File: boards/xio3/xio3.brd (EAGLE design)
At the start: 170 x 100 mm, 352 parts, among them J1 12401598E4#2A, Q1 BSS138, Q2 BSS138, Q3 BC817-16LT3G, Q4 BC817-16LT3G, Y2 FA-238 25.0000MB-K3

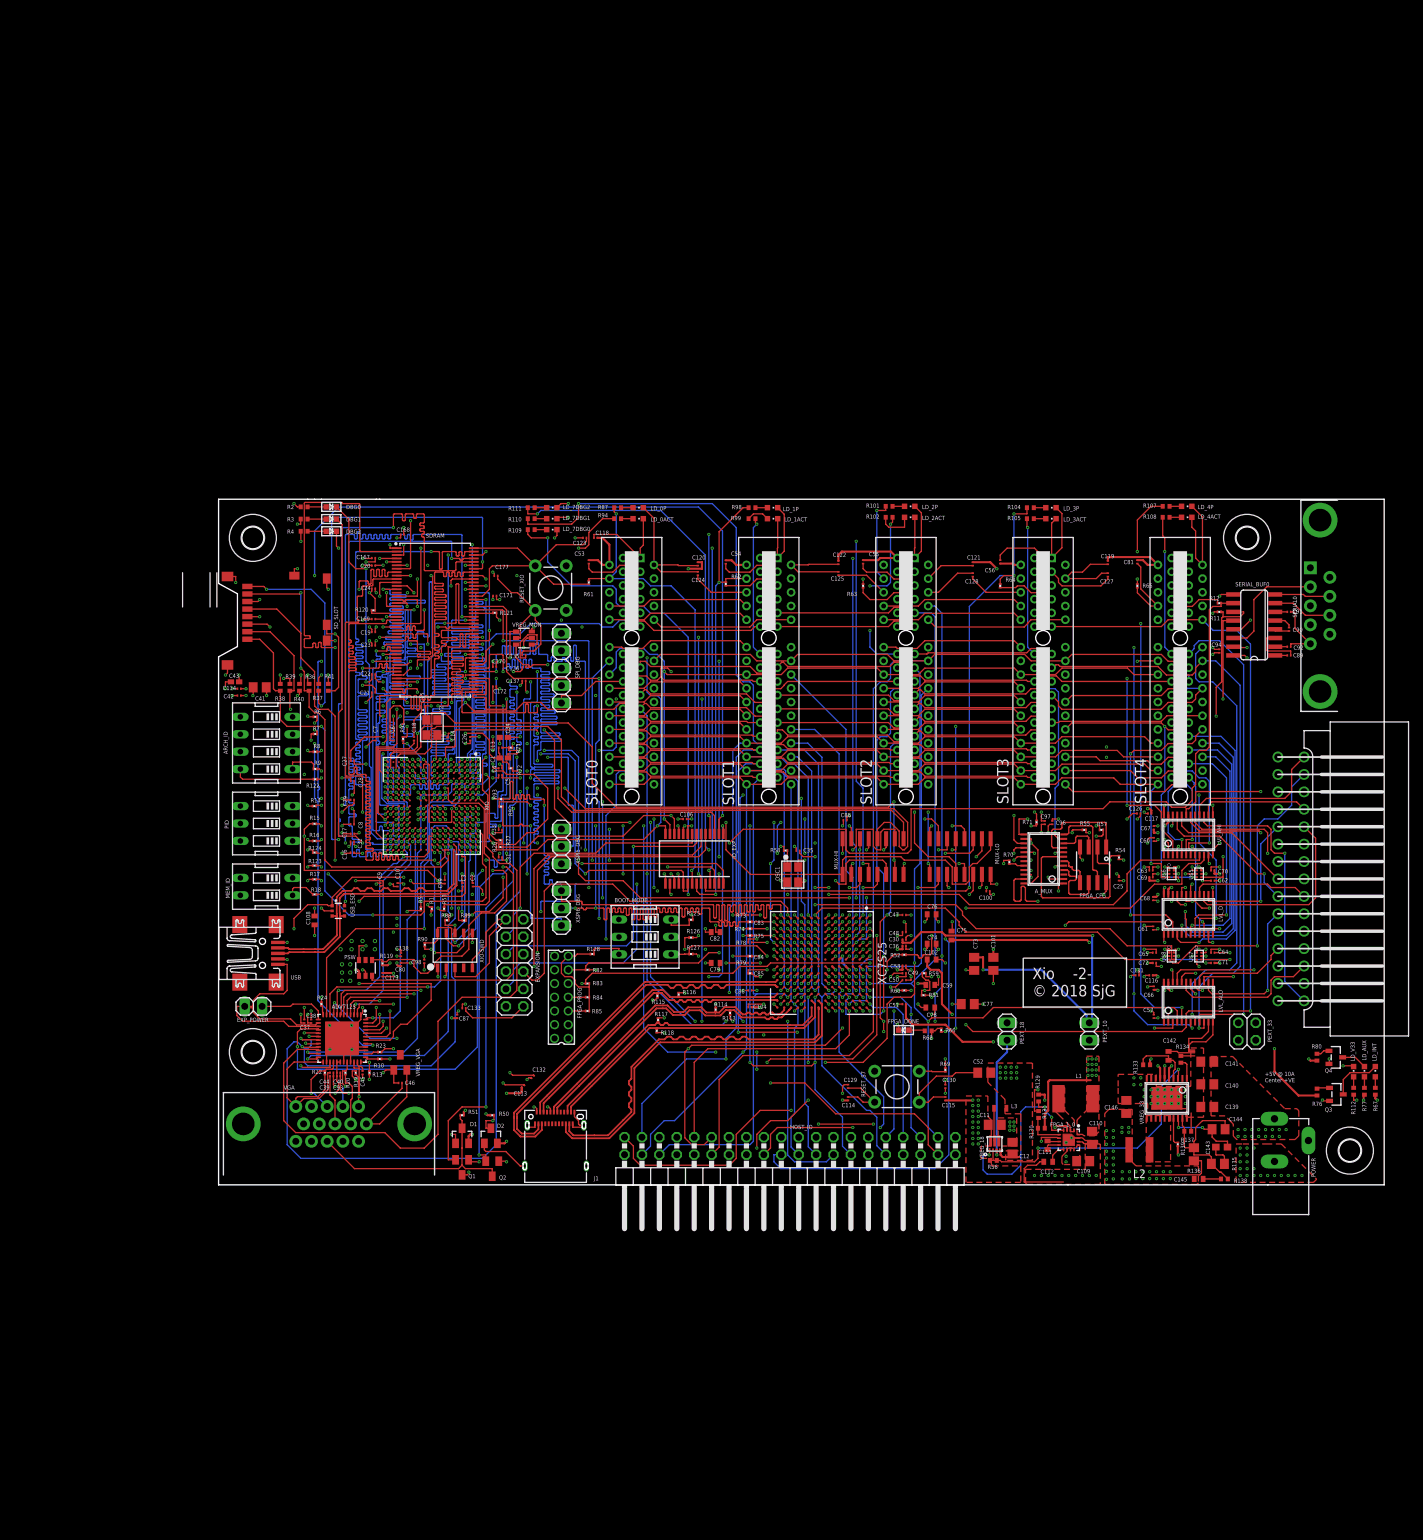
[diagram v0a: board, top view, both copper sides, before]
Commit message: Attempt at 3rd version of board, this time using a COTS FPGA board
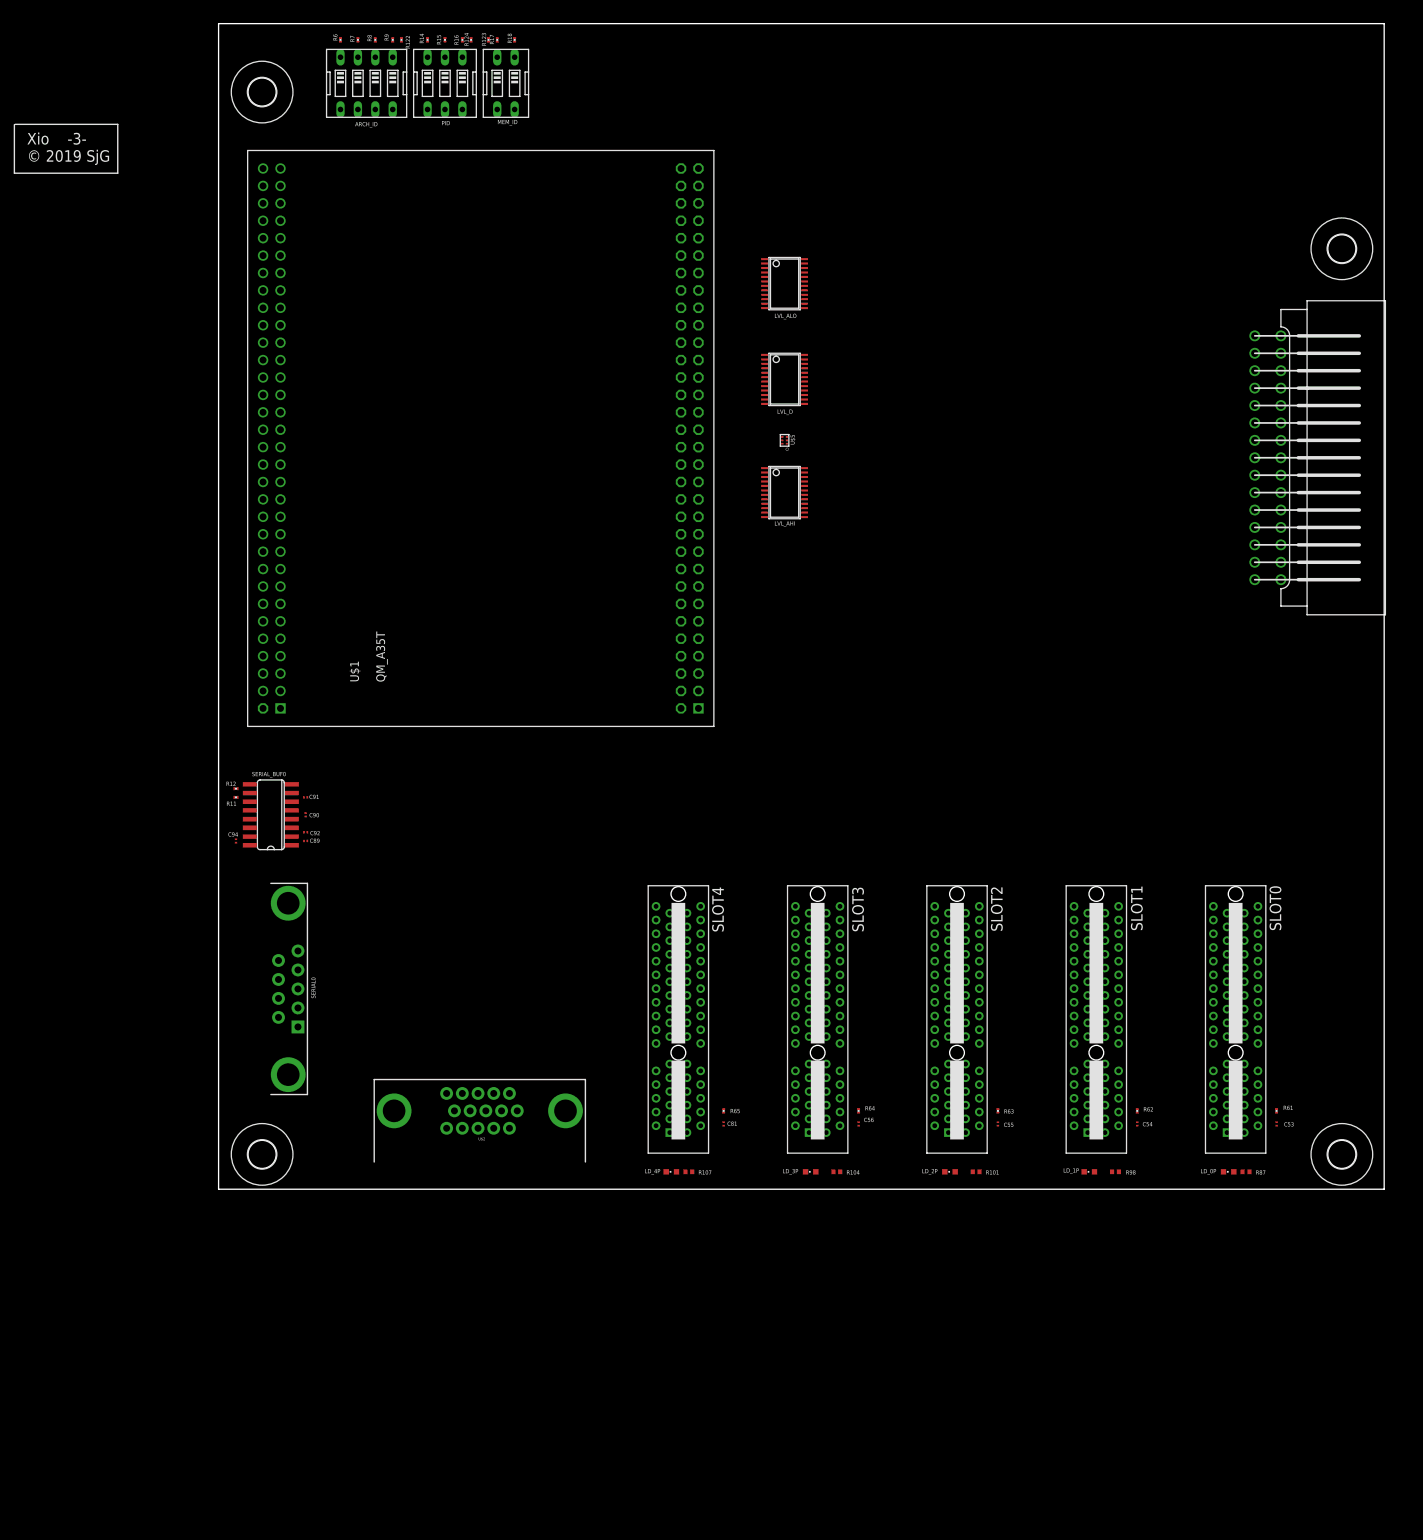
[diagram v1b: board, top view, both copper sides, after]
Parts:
- removed ADV7125: ADV7125, sjg-analog:QFN50P700X700X100-49T495
- removed A_MUX: TS3A27518EPWR, sjg-logic:TSSOP24
- removed BOOT_MODE: 209-3MS, special:EDG-03
- removed C1, C34, C43: 10uF, rcl:C0402K
- removed C10, C100, C106, C113, C114, C115, C116, C117, C118, C119, C120, C121, C122, C123, C124, C125, C126, C127, C128, C129, C13, C130, C131, C132, C133, C134, C137, C138, C16, C167, C168, C169, C170, C171, C172, C19, C2, C20, C21, C22, C23, C24, C25, C26, C27, C28, C29, C3, C31, C32, C33, C35, C38, C39, C4, C40, C45, C5, C57, C6, C60, C61, C62, C63, C64, C65, C66, C67, C68, C69, C7, C70, C71, C72, C8, C80, C87, C88, C9, C96, C98: 0.1uF, rcl:C0201
- removed C101, C73, C77: 100uF, rcl:C0805
- removed C102, C108, C59, C74, C75, C76, C78, C79, C82: 4.7uF, rcl:C0402
- removed C104, C30, C36, C47, C48, C49, C50, C51, C58, C83, C84, C85, C86: 0.47uF, rcl:C0201
- removed C109, C110, C41: 22uF, rcl:C0805
- removed C11, C139, C140, C141: 10uF, rcl:C0805
- removed C111: 0.01uF, rcl:C0402
- removed C112: 3900pF, rcl:C0402
- removed C12: 22uF, rcl:C2012
- removed C135: 120pF, rcl:C0201
- removed C136, C37, C44, C93: 0.01uF, rcl:C0201
- removed C14, C15: 16pF, rcl:C0201
- removed C142: 0.1uF, rcl:C0402
- removed C143: 1.2nF, rcl:C0603
- removed C144: 13pF, rcl:C0805
- removed C145: 560pF, rcl:C0402
- removed C146: 33uF, rcl:C0805
- removed C17, C18, C99: 2.2uF, rcl:C0201
- removed C173, C42, C46, C97: 1uF, rcl:C0201
- removed C177: 4.7uF, rcl:C0201
- removed C52: 47uF, rcl:C0805
- removed D1, D2: BAT54S, diode:SOT23
- removed DBG0, DBG1, DBG2: YELLOW_LED, microbuilder:CHIPLED_0603
- removed EXPANSION: (no value), pinhead:2X06
- removed EXP_POWER, PEXT_10, PEXT_18: (no value), pinhead:1X02
- removed FPGA_1_0: TLV62095, sjg-power:QFN50P310X310X100-16
- removed FPGA_CFG: W25Q80DVSNIG, microbuilder:SOIC8_150MIL
- removed FPGA_DONE: LTST-C191KFKT, microbuilder:CHIPLED_0603
- removed FPGA_PROG: XILINX-JTAG, sjg-con:332-14
- removed H1, H2, H4, H5: MOUNT-HOLE3.2, holes:3,2
- removed HOST_IO: (no value), pinhead:2X20/90
- removed IO_EXP: MCP23S17T-E/SS, sjg-logic:SSOP28
- removed J1: 12401598E4#2A, usb-c:AMPHENOL_12401598E4#2A
- removed L1: 1.5uH, rcl:L5650M
- removed L2: 2.2uH, sjg-inductor:RESC4137X200
- removed L3: 470nH, sjg-power:L0603
- removed LD_0ACT, LD_1ACT, LD_2ACT, LD_3ACT, LD_4ACT: LTST-C191KRKT, led:CHIPLED_0603
- removed LD_7DBG0, LD_7DBG1, LD_7DBG2: IN-S63BTA, led:CHIPLED_0603
- removed LD_AUX, LD_INT, LD_V33: LTST-S270GKT, led:CHIPLED_0603
- removed MUX-HI, MUX-LO: IDTQS3VH257, sjg-logic:SO16
- removed OSC1: 50 MHz oscillator, microbuilder:OSC_3.2X2.5MM
- removed PEXT_33: (no value), pinhead:2X02
- removed POWER: dc5vin, sjg-power:DCJ3P-14.2X11.0X9.0MM
- removed PSW: NCP380, sjg-power:SOT23-6
- removed Q1, Q2: BSS138, transistor-small-signal:SOT23
- removed Q3, Q4: BC817-16LT3G, microbuilder:SOT23-R
- removed R1, R24, R5, R53, R72: 0R, rcl:R0201
- removed R10: 560R, rcl:R0201
- removed R102, R105, R108, R109, R110, R111, R2, R3, R4, R94, R99: 130R, rcl:R0402
- removed R112: 59R, rcl:R0402
- removed R113, R114, R115, R116, R117, R118: 50R, rcl:R0201
- removed R119: 100K, rcl:R0201
- removed R120, R121, R59, R81, R82, R83, R84, R85, R88, R89, R90: 10K, rcl:R0201
- removed R125, R126, R127: 47K, rcl:R0201
- removed R128, R13, R50, R51, R58: 1K, rcl:R0201
- removed R129: 499K, rcl:R0402
- removed R130: 40.2K, rcl:R0402
- removed R131: 160K, rcl:R0402
- removed R133: 10.5R, rcl:R0402
- removed R134: 48.7K, rcl:R0402
- removed R135: 6.04K, rcl:R0805
- removed R136: 12K, rcl:R0805
- removed R137: 2.67K, rcl:R0402
- removed R138: 64.9R, rcl:R0402
- removed R139: 105K, rcl:R0201
- removed R19, R20, R22: 75R, rcl:R0201
- removed R21, R26, R27, R52, R60, R73, R74, R75, R91, R92, R93: 33R, rcl:R0201
- removed R23, R69, R70, R71, R78, R79: 4.7K, rcl:R0201
- removed R36, R37, R38, R39, R40, R41: 47K, rcl:R0402
- removed R54, R55, R57: 2.4K, rcl:R0201
- removed R56: 1M, rcl:R0402
- removed R66: 200R, rcl:R0201
- removed R67, R77: 150R, rcl:R0402
- removed R68: 100R, rcl:R0402
- removed R76, R80: 330R, rcl:R0402
- removed RESET_S7: Tac-switch, SparkFun:TACTILE-PTH
- removed RESET_XIO: TAC_SWITCH, SparkFun:TACTILE-PTH
- removed SDRAM: IS42S32160F-7TLI, sjg-sdram:SOP50P1176X120-86
- removed SD_SLOT: 5025700893, j_microsd_molex_5025700893:5025700893
- removed SPI_DBG: (no value), pinhead:1X05
- removed U$6, U$7, U$8: 74LVC1T45GWSOT866, sjg-logic:SOT886
- removed USB: MINI-USB-UX60-MB-5ST, con-hirose:UX60-MB-5ST
- removed USB_ESD: PUSB2X4YH, sjg-isolation:SOT363
- removed VGA: 15-way D, SparkFun-Connectors:DB15
- removed VREG_18: TPS62087RLTR, sjg-ti:RLT0007A
- removed VREG_33: LM21212, sjg-power:HTSSOP20
- removed VREG_MON: TPS3808G33DBVR, sjg-power:SOT23-6
- removed VREG_VGA: AD1580ARTZ, sjg-analog:SOT23
- removed XC7S25: XC7S25, sjg-xilinx:BGA196C100P14X14_1500X1500X146
- removed XIO: STM32H743-XIO, sjg-stm32:BGA289C80P17X17_1400X1400X110
- removed XIO-SWD: XIO_JTAG, sjg-stm32:SWD_DEBUG
- removed XSPI5_DBG, XSPI6_DBG: (no value), pinhead:1X03
- removed Y2: FA-238 25.0000MB-K3, microbuilder:CRYSTAL_3.2X2.5
- added H3, H6, H7, H8: MOUNT-HOLE4.1, holes:4,1
- added U$1: QM_A35T, sjg-fpga:QMTECH
- added U$2: DB15, SparkFun-Connectors:DB15
- moved SERIAL0 160.5 mm to (10.2, 29.2), turned to 90 degrees
- moved C94 146.1 mm to (2.54, 50.8)
- moved SERIAL_BUF0 146.1 mm to (7.62, 54.6)
- moved C89 145.9 mm to (12.7, 50.8)
- moved C90 145.9 mm to (12.7, 54.6)
- moved C91 145.9 mm to (12.7, 57.1)
- moved C92 145.9 mm to (12.7, 52.1)
- moved R11 145.9 mm to (2.54, 57.1)
- moved R12 145.9 mm to (2.54, 58.4)
- moved R87 133.4 mm to (149.9, 2.54), turned to 180 degrees
- moved LD_0P 129.6 mm to (147.3, 2.54), turned to 90 degrees
- moved C53 129.5 mm to (154.3, 9.53), turned to 90 degrees
- moved R18 128.0 mm to (43.2, 167.6), turned to 90 degrees
- moved R61 126.5 mm to (154.3, 11.4), turned to 270 degrees
- moved R17 125.3 mm to (40.6, 167.6), turned to 90 degrees
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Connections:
- removed net !ADDR_VALID_READ!: XC7S25.D1, XIO.M2
- removed net !ADDR_VALID_WRITE!: XC7S25.C1, XIO.M3
- removed net !GEN_CCTL!: LVL_AHI.8, XC7S25.F4
- removed net !GEN_S4!: LVL_AHI.9, XC7S25.H3
- removed net !GEN_S5!: LVL_AHI.10, XC7S25.H2
- removed net !IO_EXP_IRQ!: IO_EXP.19, IO_EXP.20, XIO.D3
- removed net !IO_EXP_SEL!: IO_EXP.11, XIO.N2
- removed net !MR!: C136.1, RESET_XIO.1, RESET_XIO.2, VREG_MON.3
- removed net !RESET!: C98.1, IO_EXP.18, R89.2, VREG_MON.1, XIO-SWD.P10, XIO.K1
- removed net !SDRAM_CAS!: SDRAM.18, XIO.D6
- removed net !SDRAM_RAS!: SDRAM.19, XIO.T7
- removed net !SDRAM_WE!: SDRAM.17, XIO.P4
- removed net !SPI_IRQ!: XC7S25.L2, XIO.D2
- removed net AGND: C1.2, C13.2, R72.2, XIO.N1, XIO.P1
- removed net BOOT0: R1.1, R5.2, XIO.E8
- removed net BOOT_M0: BOOT_MODE.1, R127.1, XC7S25.M7
- removed net BOOT_M1: BOOT_MODE.2, R126.1, XC7S25.M8
- removed net BOOT_M2: BOOT_MODE.3, R125.1, XC7S25.M9
- removed net CART_!CCTL!: CARTRIDGE.P15, LVL_AHI.16
- removed net CART_!S4!: CARTRIDGE.P1, LVL_AHI.15
- removed net CART_!S5!: CARTRIDGE.P12, LVL_AHI.14
- removed net CART_A0: CARTRIDGE.P5, LVL_ALO.21
- removed net CART_A1: CARTRIDGE.P4, LVL_ALO.20
- removed net CART_A10: CARTRIDGE.PP, LVL_AHI.19
- removed net CART_A11: CARTRIDGE.PN, LVL_AHI.18
- removed net CART_A12: CARTRIDGE.PK, LVL_AHI.17
- removed net CART_A2: CARTRIDGE.P3, LVL_ALO.19
- removed net CART_A3: CARTRIDGE.P2, LVL_ALO.18
- removed net CART_A4: CARTRIDGE.PC, LVL_ALO.17
- removed net CART_A5: CARTRIDGE.PD, LVL_ALO.16
- removed net CART_A6: CARTRIDGE.PE, LVL_ALO.15
- removed net CART_A7: CARTRIDGE.PF, LVL_ALO.14
- removed net CART_A8: CARTRIDGE.PH, LVL_AHI.21
- removed net CART_A9: CARTRIDGE.PJ, LVL_AHI.20
- removed net CART_CLK: CARTRIDGE.PS, U$5.4
- removed net CART_D0: CARTRIDGE.P10, LVL_D.21
- removed net CART_D1: CARTRIDGE.P9, LVL_D.20
- removed net CART_D2: CARTRIDGE.P8, LVL_D.19
- removed net CART_D3: CARTRIDGE.PL, LVL_D.18
- removed net CART_D4: CARTRIDGE.P6, LVL_D.17
- removed net CART_D5: CARTRIDGE.P7, LVL_D.16
- removed net CART_D6: CARTRIDGE.P11, LVL_D.15
- removed net CART_D7: CARTRIDGE.PM, LVL_D.14
- removed net CART_R/!W!: CARTRIDGE.PR, U$6.4
- removed net CART_RD4: U$7.4, XC7S25.H1
- removed net CART_RD5: U$8.4, XC7S25.J2
- removed net EXT_IO0: EXPANSION.8, IO_EXP.7
- removed net EXT_IO1: EXPANSION.10, IO_EXP.8
- removed net FLASH_CLK: A_MUX.2, R52.2
- removed net FLASH_CS: A_MUX.21, R57.1, XC7S25.C11
- removed net FLASH_D0: A_MUX.1, R60.2
- removed net FLASH_D1: A_MUX.23, XC7S25.B12
- removed net FLASH_D2: A_MUX.19, R55.1, XC7S25.D10
- removed net FLASH_D3: A_MUX.22, R54.1, XC7S25.C10
- removed net FPGA_EXT0: EXPANSION.2, XC7S25.K3
- removed net FPGA_EXT1: EXPANSION.3, XC7S25.J4
- removed net FPGA_EXT2: EXPANSION.4, XC7S25.J3
- removed net FPGA_EXT3: EXPANSION.5, XC7S25.M1
- removed net FPGA_EXT4: EXPANSION.6, XC7S25.L1
- removed net FPGA_EXT5: EXPANSION.7, XC7S25.M3
- removed net HOST_CTL0: HOST_IO.2, XC7S25.N10
- removed net HOST_CTL1: HOST_IO.4, XC7S25.N11
- removed net HOST_DIR0: HOST_IO.22, LVL_D.2, XC7S25.B6
- removed net HOST_DIR1: HOST_IO.24, XC7S25.D3
- removed net HOST_DIR2: HOST_IO.26, XC7S25.C3
- removed net HOST_DIR3: HOST_IO.28, XC7S25.A4
- removed net HOST_DIR4: HOST_IO.30, XC7S25.A3
- removed net LCD_B0: ADV7125.16, XIO.D11
- removed net LCD_B1: ADV7125.17, XIO.E10
- removed net LCD_B2: ADV7125.18, XIO.D10
- removed net LCD_B3: ADV7125.19, XIO.B10
- removed net LCD_B4: ADV7125.20, XIO.C8
- removed net LCD_B5: ADV7125.21, XIO.B8
- removed net LCD_B6: ADV7125.22, XIO.A8
- removed net LCD_B7: ADV7125.23, XIO.C7
- removed net LCD_BLANK: ADV7125.11, XIO.D7
- removed net LCD_CLK: ADV7125.24, XIO.F16
- removed net LCD_G0: ADV7125.3, XIO.N14
- removed net LCD_G1: ADV7125.4, XIO.N13
- removed net LCD_G2: ADV7125.5, XIO.M14
- removed net LCD_G3: ADV7125.6, XIO.L14
- removed net LCD_G4: ADV7125.7, XIO.K14
- removed net LCD_G5: ADV7125.8, XIO.J14
- removed net LCD_G6: ADV7125.9, XIO.J15
- removed net LCD_G7: ADV7125.10, XIO.H17
- removed net LCD_HS: Q2.2, XIO.H1
- removed net LCD_R0: ADV7125.41, XIO.P5
- removed net LCD_R1: ADV7125.42, XIO.N6
- removed net LCD_R2: ADV7125.43, XIO.P6
- removed net LCD_R3: ADV7125.44, XIO.T6
- removed net LCD_R4: ADV7125.45, XIO.U6
- removed net LCD_R5: ADV7125.46, XIO.U7
- removed net LCD_R6: ADV7125.47, XIO.R12
- removed net LCD_R7: ADV7125.48, XIO.N15
- removed net LCD_VS: Q1.2, XIO.H2
- removed net LX_CLK: OSC1.3, XC7S25.G4
- removed net LX_MISC: J1.A5, XC7S25.M10
- removed net LX_RC_N: J1.B11, XC7S25.P11
- removed net LX_RC_P: J1.B10, XC7S25.P10
- removed net LX_RD_N: J1.B2, XC7S25.H14
- removed net LX_RD_P: J1.B3, XC7S25.H13
- removed net LX_TC_N: J1.A7, R113.1, XC7S25.M14
- removed net LX_TC_P: J1.A6, R114.1, XC7S25.N14
- removed net LX_TD0_N: J1.A3, R115.1, XC7S25.P13
- removed net LX_TD0_P: J1.A2, R116.1, XC7S25.P12
- removed net LX_TD1_N: J1.A10, R117.1, XC7S25.J14
- removed net LX_TD1_P: J1.A11, R118.1, XC7S25.J13
- removed net N$1: PSW.3, XIO.A14
- removed net N$10: ADV7125.38, R23.1
- removed net N$102: LD_4ACT.A, R108.2
- removed net N$103: LD_7DBG0.A, R109.2
- removed net N$104: LD_7DBG1.A, R110.2
- removed net N$105: LD_7DBG2.A, R111.2
- removed net N$106: LD_V33.A, R112.2
- removed net N$108: C143.1, C144.1, VREG_33.18
- removed net N$109: C143.2, R135.2
- removed net N$110: C144.2, R135.1, R136.2, R137.1, R138.2, VREG_33.19
- removed net N$113: C145.2, R138.1
- removed net N$12: DBG0.A, R2.2
- removed net N$13: DBG0.C, XIO.R15
- removed net N$14: DBG1.C, XIO.R16
- removed net N$15: DBG2.C, XIO.R17
- removed net N$16: DBG1.A, R3.2
- removed net N$17: ADV7125.37, R10.2
- removed net N$18: ADV7125.12, R24.2
- removed net N$19: DBG2.A, R4.2
- removed net N$2: R121.2, SDRAM.67
- removed net N$3: R60.1, XC7S25.B11
- removed net N$4: A_MUX.4, FPGA_CFG.6
- removed net N$5: OSC1.1, R58.2
- removed net N$50: BOOT_MODE.4, BOOT_MODE.5, BOOT_MODE.6, R128.2
- removed net N$51: R52.1, XC7S25.A8
- removed net N$55: R66.1, R68.2, XC7S25.P9
- removed net N$56: FPGA_DONE.A, R68.1
- removed net N$57: R26.2, XIO.C3
- removed net N$58: CARTRIDGE.PA, U$7.3
- removed net N$59: CARTRIDGE.P14, U$8.3
- removed net N$6: ADV7125.36, C46.1, R13.1, VREG_VGA.1
- removed net N$60: C135.1, VREG_MON.4
- removed net N$61: R27.2, XIO.E5
- removed net N$62: A_MUX.6, FPGA_CFG.5
- removed net N$63: A_MUX.7, FPGA_CFG.2
- removed net N$64: C111.1, FPGA_1_0.7
- removed net N$65: PSW.4, R119.2, XIO.C11
- removed net N$66: A_MUX.9, FPGA_CFG.1
- removed net N$67: A_MUX.10, FPGA_CFG.3
- removed net N$68: A_MUX.12, FPGA_CFG.7
- removed net N$69: R69.1, RESET_S7.3, RESET_S7.4, XC7S25.L7
- removed net N$7: R120.1, SDRAM.20
- removed net N$70: R78.1, XC7S25.P8
- removed net N$71: A_MUX.20, R70.1
- removed net N$72: C111.2, FPGA_1_0.8
- removed net N$73: FPGA_1_0.1, FPGA_1_0.2, L1.1
- removed net N$75: C142.1, R133.1, VREG_33.4
- removed net N$76: LD_INT.A, R67.2
- removed net N$77: R79.1, XC7S25.N7
- removed net N$78: Q3.1, R76.1
- removed net N$79: FPGA_1_0.5, R130.2, R131.1
- removed net N$8: ADV7125.35, C45.2
- removed net N$80: LD_INT.C, Q3.3
- removed net N$81: LD_AUX.A, R77.2
- removed net N$83: R134.2, VREG_33.1
- removed net N$84: LD_0ACT.A, R94.2
- removed net N$85: Q4.1, R80.1
- removed net N$86: LD_AUX.C, Q4.3
- removed net N$9: L3.1, VREG_18.6
- removed net N$92: LD_1ACT.A, R99.2
- removed net N$95: LD_2ACT.A, R102.2
- removed net N$98: C112.1, FPGA_1_0.9
- removed net N$99: LD_3ACT.A, R105.2
- removed net PDR_ON: R53.2, XIO.E7
- removed net PGOOD33: R139.2, VREG_33.17
- removed net PGOOD_10: FPGA_1_0.4, R129.2, VREG_18.1
- removed net PGOOD_18: R56.1, VREG_18.2, VREG_33.3
- removed net S7_DBG0: R109.1, XC7S25.H4
- removed net S7_DBG1: R110.1, XC7S25.J1
- removed net S7_DBG2: R111.1, XC7S25.K4
- removed net SD0: R36.1, SD_SLOT.P$7, XIO.E13
- removed net SD1: R37.1, SD_SLOT.P$8, XIO.E14
- removed net SD2: R38.1, SD_SLOT.P$1, XIO.A13
- removed net SD3: R39.1, SD_SLOT.P$2, XIO.B13
- removed net SDCD: R41.1, SD_SLOT.DTCT, XIO.E3
- removed net SDCLK: SD_SLOT.P$5, XIO.C12
- removed net SDCMD: R40.1, SD_SLOT.P$3, XIO.D12
- removed net SDRAM_A0: SDRAM.25, XIO.G4
- removed net SDRAM_A1: SDRAM.26, XIO.G3
- removed net SDRAM_A10: SDRAM.24, XIO.T8
- removed net SDRAM_A11: SDRAM.21, XIO.U8
- removed net SDRAM_A12: SDRAM.69, XIO.H16
- removed net SDRAM_A2: SDRAM.27, XIO.G1
- removed net SDRAM_A3: SDRAM.60, XIO.H4
- removed net SDRAM_A4: SDRAM.61, XIO.J5
- removed net SDRAM_A5: SDRAM.62, XIO.J4
- removed net SDRAM_A6: SDRAM.63, XIO.R7
- removed net SDRAM_A7: SDRAM.64, XIO.P7
- removed net SDRAM_A8: SDRAM.65, XIO.P8
- removed net SDRAM_A9: SDRAM.66, XIO.R9
- removed net SDRAM_BA0: SDRAM.22, XIO.H14
- removed net SDRAM_BA1: SDRAM.23, XIO.G14
- removed net SDRAM_CLK: SDRAM.68, XIO.F15
- removed net SDRAM_D0: SDRAM.2, XIO.P16
- removed net SDRAM_D1: SDRAM.4, XIO.P15
- removed net SDRAM_D10: SDRAM.77, XIO.T10
- removed net SDRAM_D11: SDRAM.79, XIO.U10
- removed net SDRAM_D12: SDRAM.80, XIO.R11
- removed net SDRAM_D13: SDRAM.82, XIO.U16
- removed net SDRAM_D14: SDRAM.83, XIO.T17
- removed net SDRAM_D15: SDRAM.85, XIO.T16
- removed net SDRAM_D16: SDRAM.31, XIO.T13
- removed net SDRAM_D17: SDRAM.33, XIO.R13
- removed net SDRAM_D18: SDRAM.34, XIO.P13
- removed net SDRAM_D19: SDRAM.36, XIO.P14
- removed net SDRAM_D2: SDRAM.5, XIO.D13
- removed net SDRAM_D20: SDRAM.37, XIO.R14
- removed net SDRAM_D21: SDRAM.39, XIO.D16
- removed net SDRAM_D22: SDRAM.40, XIO.B17
- removed net SDRAM_D23: SDRAM.42, XIO.B16
- removed net SDRAM_D24: SDRAM.45, XIO.A16
- removed net SDRAM_D25: SDRAM.47, XIO.A15
- removed net SDRAM_D26: SDRAM.48, XIO.B15
- removed net SDRAM_D27: SDRAM.50, XIO.C14
- removed net SDRAM_D28: SDRAM.51, XIO.A2
- removed net SDRAM_D29: SDRAM.53, XIO.B3
- removed net SDRAM_D3: SDRAM.7, XIO.E12
- removed net SDRAM_D30: SDRAM.54, XIO.E2
- removed net SDRAM_D31: SDRAM.56, XIO.F3
- removed net SDRAM_D4: SDRAM.8, XIO.U9
- removed net SDRAM_D5: SDRAM.10, XIO.T9
- removed net SDRAM_D6: SDRAM.11, XIO.P9
- removed net SDRAM_D7: SDRAM.13, XIO.N9
- removed net SDRAM_D8: SDRAM.74, XIO.P10
- removed net SDRAM_D9: SDRAM.76, XIO.R10
- removed net SDRAM_DQM0: SDRAM.16, XIO.C4
- removed net SDRAM_DQM1: SDRAM.71, XIO.B4
- removed net SDRAM_DQM2: SDRAM.28, XIO.A4
- removed net SDRAM_DQM3: SDRAM.59, XIO.A3
- removed net SPI_MUX_IN: A_MUX.14, A_MUX.24, R71.1, XIO.P2
- removed net STMDATA_A0: MUX-LO.2, XC7S25.B3
- removed net STMDATA_A1: MUX-LO.5, XC7S25.A2
- removed net STMDATA_A2: MUX-LO.11, XC7S25.B5
- removed net STMDATA_A3: MUX-LO.14, XC7S25.A5
- removed net STMDATA_A4: MUX-HI.2, XC7S25.B2
- removed net STMDATA_A5: MUX-HI.5, XC7S25.B1
- removed net STMDATA_A6: MUX-HI.11, XC7S25.C5
- removed net STMDATA_A7: MUX-HI.14, XC7S25.C4
- removed net STMDATA_B0: MUX-LO.3, XC7S25.E4
- removed net STMDATA_B1: MUX-LO.6, XC7S25.D4
- removed net STMDATA_B2: MUX-LO.10, XC7S25.F3
- removed net STMDATA_B3: MUX-LO.13, XC7S25.F2
- removed net STMDATA_B4: MUX-HI.3, XC7S25.G1
- removed net STMDATA_B5: MUX-HI.6, XC7S25.F1
- removed net STMDATA_B6: MUX-HI.10, XC7S25.E2
- removed net STMDATA_B7: MUX-HI.13, XC7S25.D2
- removed net STM_MUX_CTL: MUX-HI.1, MUX-LO.1, XIO.M4
- removed net STM_MUX_D0: MUX-LO.4, XIO.N5
- removed net STM_MUX_D1: MUX-LO.7, XIO.N4
- removed net STM_MUX_D2: MUX-LO.9, XIO.N3
- removed net STM_MUX_D3: MUX-LO.12, XIO.U2
- removed net STM_MUX_D4: MUX-HI.4, XIO.U3
- removed net STM_MUX_D5: MUX-HI.7, XIO.T3
- removed net STM_MUX_D6: MUX-HI.9, XIO.R3
- removed net STM_MUX_D7: MUX-HI.12, XIO.R5
- removed net SW_OUT: L2.1, VREG_33.11, VREG_33.12, VREG_33.13, VREG_33.14, VREG_33.15, VREG_33.16
- removed net TCK: FPGA_PROG.6, R83.2, XC7S25.A7
- removed net TDI: FPGA_PROG.10, R85.2, XC7S25.P7
- removed net TDO: FPGA_PROG.8, R84.2, XC7S25.P6
- removed net TMS: FPGA_PROG.4, R82.2, XC7S25.M6
- removed net VCCAUX: C12.1, C51.1, C52.1, C58.1, C59.1, L3.2, PEXT_18.1, PEXT_18.2, R80.2, VREG_18.3, VREG_18.4, XC7S25.B8, XC7S25.F10, XC7S25.F8, XC7S25.H10, XC7S25.K10, XC7S25.L9
- removed net VCCINT: C101.1, C102.1, C104.1, C110.1, C30.1, C36.1, C73.1, C74.1, C75.1, FPGA_1_0.16, L1.2, PEXT_10.1, PEXT_10.2, R130.1, R76.2, XC7S25.D6, XC7S25.D8, XC7S25.E5, XC7S25.E7, XC7S25.E9, XC7S25.F6, XC7S25.G5, XC7S25.G9, XC7S25.H6, XC7S25.J5, XC7S25.J9, XC7S25.K6, XC7S25.K8
- removed net VGA_B: ADV7125.28, R22.1, VGA.3
- removed net VGA_G: ADV7125.32, R20.1, VGA.2
- removed net VGA_HS: D1.3, Q2.3, R51.2, VGA.13
- removed net VGA_R: ADV7125.34, R19.1, VGA.1
- removed net VGA_VS: D2.3, Q1.3, R50.2, VGA.14
- removed net XIO_CLK_IN: C14.1, XIO.J1, Y2.2
- removed net XIO_CLK_OUT: C15.1, XIO.J2, Y2.1
- removed net XIO_RX: XIO-SWD.P8, XIO.F13
- removed net XIO_SWDCLK: XIO-SWD.P4, XIO.B14
- removed net XIO_SWDIO: R90.2, XIO-SWD.P2, XIO.C15
- removed net XIO_TX: R88.2, XIO-SWD.P6, XIO.F14
- removed net XIO_USB_ID: USB.4, USB_ESD.1, XIO.D14
- removed net XIO_USB_N: USB.2, USB_ESD.3, XIO.E17
- removed net XIO_USB_P: USB.3, USB_ESD.4, XIO.E16
- removed net XIO_USB_VBUS: C108.1, PSW.6, USB.1, USB_ESD.6, XIO.D15
- removed net XIO_VCAP1: C18.1, XIO.U11
- removed net XIO_VCAP2: C17.1, XIO.D17
- removed net XIO_VCAP3: C99.1, XIO.A7
- removed net XIO_VDDA: C1.1, C13.1, R21.1, XIO.L1, XIO.M1
- removed net XSPI5_MISO: R91.2, XC7S25.P3, XSPI5_DBG.2
- removed net XSPI5_MISO_R: R91.1, XIO.K4
- removed net XSPI5_MOSI: R74.1, XIO.L4, XSPI5_DBG.3
- removed net XSPI5_MOSI_R: R74.2, XC7S25.L3
- removed net XSPI5_SCK: R75.1, XIO.K3, XSPI5_DBG.1
- removed net XSPI5_SCK_R: R75.2, XC7S25.P4
- removed net XSPI6_MISO: R73.1, XIO.C9, XSPI6_DBG.2
- removed net XSPI6_MISO_R: R73.2, XC7S25.P2
- removed net XSPI6_MOSI: R93.2, XC7S25.N1, XSPI6_DBG.3
- removed net XSPI6_MOSI_R: R93.1, XIO.D8
- removed net XSPI6_SCK: R92.2, XC7S25.M2, XSPI6_DBG.1
- removed net XSPI6_SCK_R: R92.1, XIO.D9
- net +3V3: no longer ADV7125.13, ADV7125.29, ADV7125.30, A_MUX.16, A_MUX.18, A_MUX.8, C10.1, C100.1, C106.2, C123.1, C124.1, C125.1, C126.1, C127.1, C128.1, C129.1, C130.1, C131.1, C132.1, C133.1, C134.2, C137.1, C138.1, C145.1, C146.1, C16.1, C167.1, C168.1, C169.1, C170.1, C171.1, C172.1, C177.1, C19.1, C2.1, C20.1, C21.1, C22.1, C23.1, C24.1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
- net +5V: no longer C109.1, C11.1, C113.1, C114.1, C115.1, C116.1, C117.1, C118.1, C119.1, C120.1, C121.1, C122.1, C139.1, C140.1, C141.1, C173.1, C66.1, C67.1, C68.1, C69.1, C70.1, C71.1, C72.1, C80.1, C87.1, D1.2, D2.2, FPGA_1_0.10, FPGA_1_0.11, FPGA_1_0.12, FPGA_1_0.13, FPGA_1_0.3, POWER.+, PSW.1, R119.1, R129.1, R133.2, R139.1, R50.1, R51.1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
- net ARCH0: no longer IO_EXP.1
- net ARCH1: no longer IO_EXP.2
- net ARCH2: no longer IO_EXP.3
- net ARCH3: no longer IO_EXP.4
- net GND: no longer ADV7125.1, ADV7125.14, ADV7125.15, ADV7125.2, ADV7125.25, ADV7125.26, ADV7125.27, ADV7125.31, ADV7125.33, ADV7125.39, ADV7125.40, ADV7125.49, A_MUX.17, A_MUX.5, C10.2, C100.2, C101.2, C102.2, C104.2, C106.1, C108.2, C109.2, C11.2, C110.2, C112.2, C113.2, C114.2, C115.2, C116.2, C117.2, C118.2, C119.2, C12.2, C120.2, C121.2, C122.2, C123.2, C124.2, C125.2, C126.2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
- net HOST_!EXTSEL!: no longer HOST_IO.35, XC7S25.J11
- net HOST_!HALT!: no longer HOST_IO.37, XC7S25.J12
- net HOST_!IRQ!: no longer HOST_IO.39, XC7S25.K11
- net HOST_!MPD!: no longer HOST_IO.32, XC7S25.K12
- net HOST_!REF!: no longer HOST_IO.34, XC7S25.M11
- net HOST_!RST!: no longer HOST_IO.36, XC7S25.M12
- net HOST_A0: no longer HOST_IO.1, LVL_ALO.3, R59.2, R81.1, XC7S25.B10, XIO.U5
- net HOST_A1: no longer HOST_IO.3, LVL_ALO.4, XC7S25.A10, XIO.T5
- net HOST_A10: no longer HOST_IO.21, LVL_AHI.5, XC7S25.D13, XIO.P11
- net HOST_A11: no longer HOST_IO.23, LVL_AHI.6, XC7S25.G14, XIO.P12
- net HOST_A12: no longer HOST_IO.25, LVL_AHI.7, XC7S25.F14, XIO.T14
- net HOST_A13: no longer HOST_IO.27, XC7S25.F13, XIO.U14
- net HOST_A14: no longer HOST_IO.29, XC7S25.E13, XIO.U15
- net HOST_A15: no longer HOST_IO.31, XC7S25.D14, XIO.T15
- net HOST_A2: no longer HOST_IO.5, LVL_ALO.5, XC7S25.A12, XIO.R6
- net HOST_A3: no longer HOST_IO.7, LVL_ALO.6, XC7S25.A13, XIO.C6
- net HOST_A4: no longer HOST_IO.9, LVL_ALO.7, XC7S25.B13, XIO.B7
- net HOST_A5: no longer HOST_IO.11, LVL_ALO.8, XC7S25.B14, XIO.A5
- net HOST_A6: no longer HOST_IO.13, LVL_ALO.9, XC7S25.C12, XIO.B5
- net HOST_A7: no longer HOST_IO.15, LVL_ALO.10, XC7S25.F12, XIO.C5
- net HOST_A8: no longer HOST_IO.17, LVL_AHI.3, XC7S25.E12, XIO.D5
- net HOST_A9: no longer HOST_IO.19, LVL_AHI.4, XC7S25.D12, XIO.D4
- net HOST_CLK: no longer HOST_IO.33, U$5.3, XC7S25.E11
- net HOST_D0: no longer HOST_IO.6, LVL_D.3, XC7S25.C14
- net HOST_D1: no longer HOST_IO.8, LVL_D.4, XC7S25.G11
- net HOST_D2: no longer HOST_IO.10, LVL_D.5, XC7S25.F11
- net HOST_D3: no longer HOST_IO.12, LVL_D.6, XC7S25.H11
- net HOST_D4: no longer HOST_IO.14, LVL_D.7, XC7S25.H12
- net HOST_D5: no longer HOST_IO.16, LVL_D.8, XC7S25.M13
- net HOST_D6: no longer HOST_IO.18, LVL_D.9, XC7S25.L12
- net HOST_D7: no longer HOST_IO.20, LVL_D.10, XC7S25.L13
- net HOST_R/!W!: no longer HOST_IO.38, U$6.3, XC7S25.L14
- net MCU_CTS: no longer XIO.B12
- net MCU_RTS: no longer XIO.A12
- net MCU_RX: no longer XIO.B11
- net MCU_TX: no longer XIO.A11
- net MEM0: no longer IO_EXP.5
- net MEM1: no longer IO_EXP.6
- net PID0: no longer IO_EXP.26
- net PID1: no longer IO_EXP.27
- net PID2: no longer IO_EXP.28
- net S0_PRESENT: no longer IO_EXP.21
- net S1_PRESENT: no longer IO_EXP.22
- net S2_PRESENT: no longer IO_EXP.23
- net S3_PRESENT: no longer IO_EXP.24
- net S4_PRESENT: no longer IO_EXP.25
- net SPI_CLK: no longer A_MUX.11, IO_EXP.12, R26.1, SPI_DBG.1
- net SPI_IRQ0: no longer SPI_DBG.4, XC7S25.L5, XIO.H15
- net SPI_IRQ1: no longer XC7S25.N4, XIO.G15
- net SPI_IRQ2: no longer XC7S25.P5, XIO.A10
- net SPI_IRQ3: no longer XC7S25.M4, XIO.A9
- net SPI_IRQ4: no longer XC7S25.M5, XIO.B9
- net SPI_MISO: no longer A_MUX.15, IO_EXP.13, SPI_DBG.2, XIO.D1
- net SPI_MOSI: no longer A_MUX.13, IO_EXP.14, R27.1, SPI_DBG.3
- net SPI_SS0: no longer R94.1, SPI_DBG.5, XIO.L2
- net SPI_SS1: no longer R99.1, XIO.T4
- net SPI_SS2: no longer R102.1, XIO.U4
- net SPI_SS3: no longer R105.1, XIO.C2
- net SPI_SS4: no longer R108.1, XIO.C1
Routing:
- net GND: track 872.8 -> 0.00 mm, vias 350 -> 0
- net +3V3: track 338.6 -> 0.00 mm, vias 223 -> 0
- net HOST_A0: track 329.9 -> 0.00 mm, vias 8 -> 0
- net HOST_A7: track 284.6 -> 0.00 mm, vias 7 -> 0
- net HOST_A12: track 284.4 -> 0.00 mm, vias 10 -> 0
- net HOST_A3: track 280.4 -> 0.00 mm, vias 4 -> 0
- net HOST_A10: track 280.0 -> 0.00 mm, vias 7 -> 0
- net HOST_A1: track 272.6 -> 0.00 mm, vias 5 -> 0
- net HOST_A2: track 272.0 -> 0.00 mm, vias 7 -> 0
- net HOST_A15: track 271.7 -> 0.00 mm, vias 6 -> 0
- net HOST_A6: track 270.1 -> 0.00 mm, vias 5 -> 0
- net VCCINT: track 261.8 -> 0.00 mm, vias 34 -> 0
- net HOST_A5: track 256.2 -> 0.00 mm, vias 4 -> 0
- net HOST_A11: track 256.2 -> 0.00 mm, vias 6 -> 0
- net HOST_A4: track 253.1 -> 0.00 mm, vias 7 -> 0
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- removed copper zone on layer 1, net +3V3
- removed copper zone on layer 15, net +3V3
- removed copper zone on layer 1, net +5V
- removed copper zone on layer 14, net +5V
- removed copper zone on layer 1, net GND
- removed copper zone on layer 2, net GND
- removed copper zone on layer 1, net N$73
- removed copper zone on layer 1, net SW_OUT
- removed copper zone on layer 1, net VCCAUX
- removed copper zone on layer 14, net VCCAUX
- removed copper zone on layer 1, net VCCINT
- removed copper zone on layer 14, net VCCINT
- removed copper zone on layer 14, net XIO_USB_VBUS
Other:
- board size 170 x 100 mm -> 170 x 170 mm
- board text added: "Xio -3- © 2019 SjG"
- board text removed: "+5V @ 10A Center +VE"
- board text removed: "Xio -2- © 2018 SjG"

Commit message: Start to connect up the cartridge port
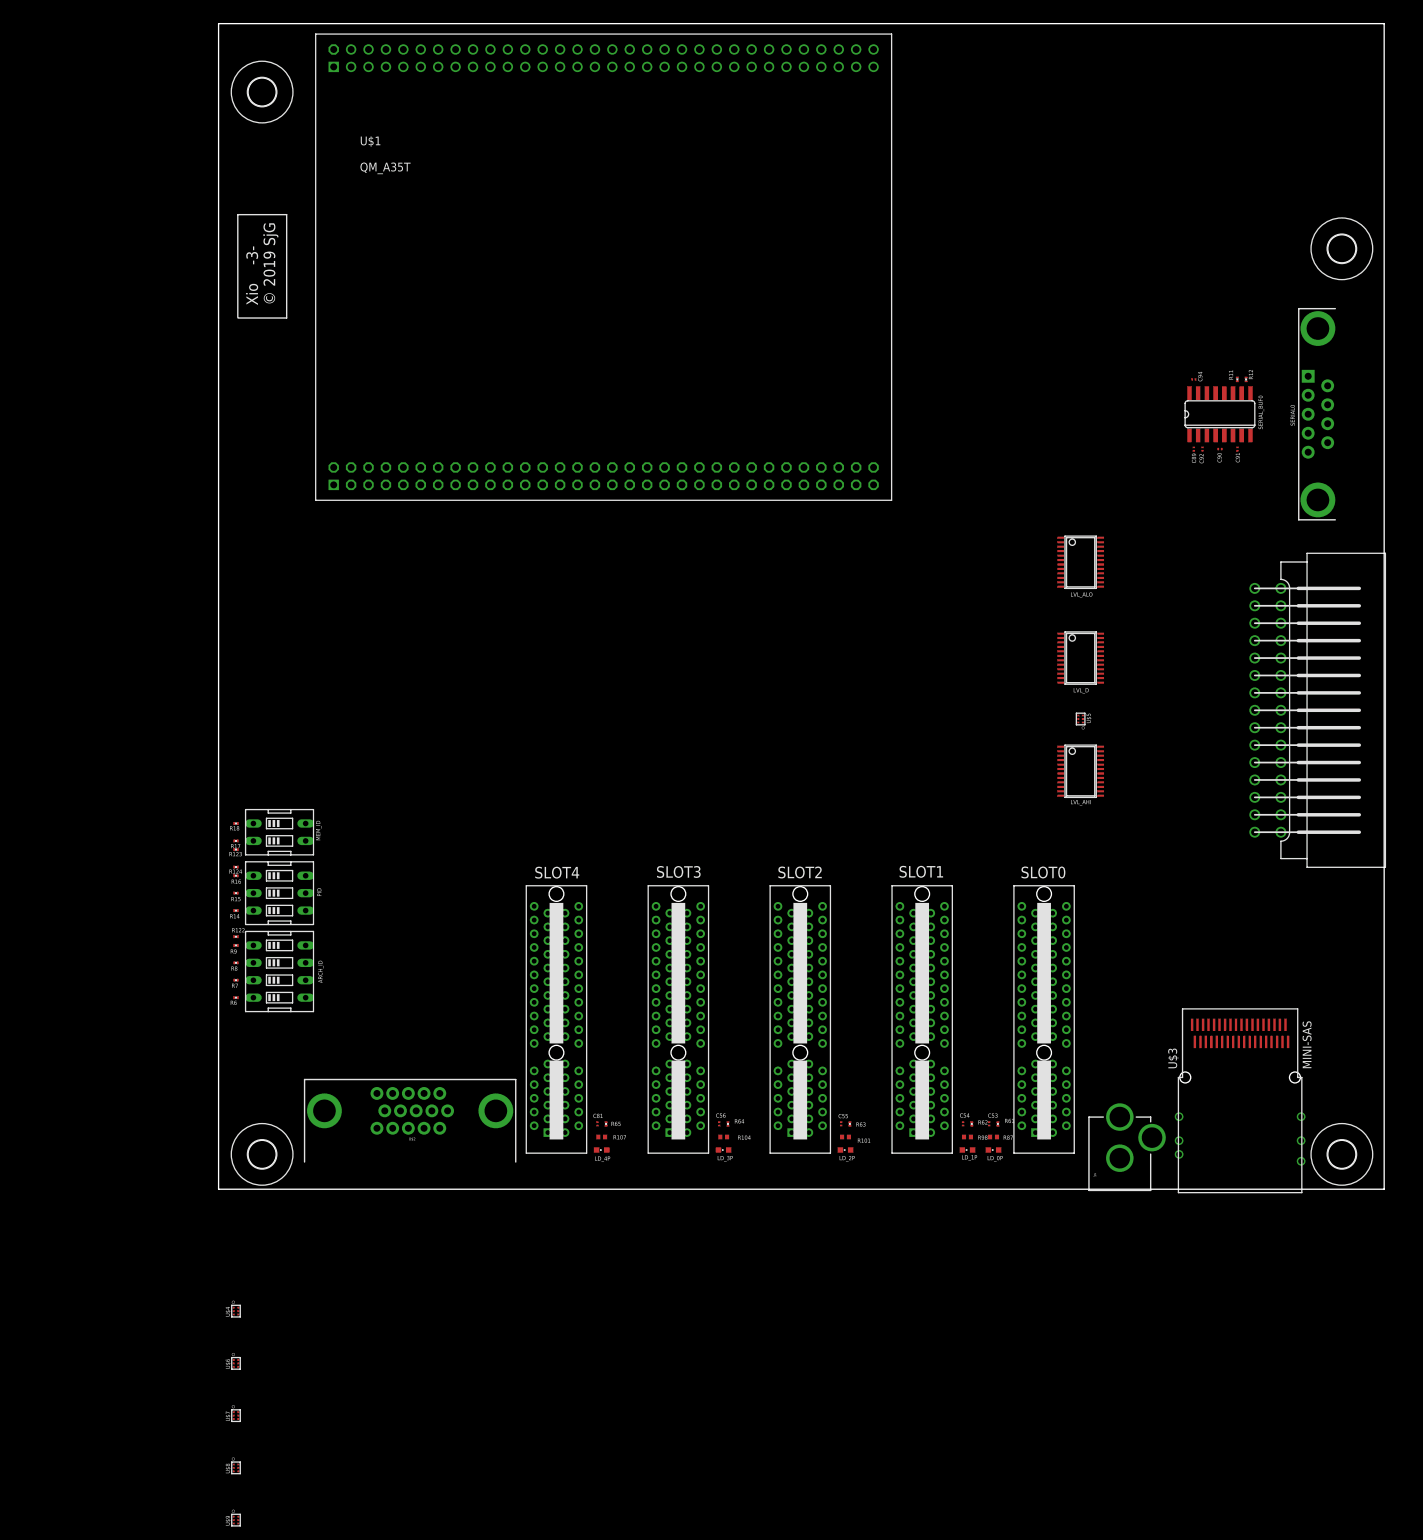
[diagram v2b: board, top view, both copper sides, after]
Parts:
- added J1: POWER_JACKPTH, SparkFun:POWER_JACK_PTH
- added U$3: MINI-SAS, sjg-con:MINI-SAS
- added U$4, U$6, U$7, U$8, U$9: 74LVC1T45GWSOT866, sjg-logic:SOT886
- moved SERIAL0 172.0 mm to (160.3, 113.0), turned to 270 degrees
- moved R12 159.0 mm to (149.9, 118.1), turned to 270 degrees
- moved R11 158.3 mm to (148.6, 118.1), turned to 270 degrees
- moved C94 155.1 mm to (142.2, 118.1), turned to 180 degrees
- moved SERIAL_BUF0 150.3 mm to (146.1, 113.0), turned to 0 degrees
- moved C91 145.1 mm to (148.6, 108.0), turned to 270 degrees
- moved C90 143.6 mm to (146.1, 108.0), turned to 180 degrees
- moved C92 142.2 mm to (143.5, 108.0), turned to 270 degrees
- moved C89 141.6 mm to (142.2, 108.0), turned to 90 degrees
- moved R6 140.5 mm to (2.54, 27.9), turned to 180 degrees
- moved R7 138.3 mm to (2.54, 30.5), turned to 180 degrees
- moved R8 136.1 mm to (2.54, 33.0), turned to 180 degrees
- moved R9 134.0 mm to (2.54, 35.6), turned to 180 degrees
- moved R122 133.0 mm to (2.54, 36.8), turned to 0 degrees
- moved ARCH_ID 130.2 mm to (8.89, 31.8), turned to 270 degrees
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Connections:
- new net !H_CCTL!: CARTRIDGE.P15
- new net !H_EXTSEL!: U$3.PB13
- new net !H_HALT!: U$3.PA14
- new net !H_IRQ!: U$3.PB14
- new net !H_MPD!: U$3.PA15
- new net !H_RST!: U$3.PA17
- new net !H_S4!: CARTRIDGE.P1
- new net !H_S5!: CARTRIDGE.P12
- new net H_A0: CARTRIDGE.P5, LVL_ALO.21, U$3.PA1
- new net H_A1: CARTRIDGE.P4, LVL_ALO.20, U$3.PB1
- new net H_A10: CARTRIDGE.PP, LVL_AHI.19, U$3.PA6
- new net H_A11: CARTRIDGE.PN, LVL_AHI.18, U$3.PB6
- new net H_A12: CARTRIDGE.PK, LVL_AHI.17, U$3.PA7
- new net H_A13: LVL_AHI.16, U$3.PB7
- new net H_A14: LVL_AHI.15, U$3.PA8
- new net H_A15: LVL_AHI.14, U$3.PB8
- new net H_A2: CARTRIDGE.P3, LVL_ALO.19, U$3.PA2
- new net H_A3: CARTRIDGE.P2, LVL_ALO.18, U$3.PB2
- new net H_A4: CARTRIDGE.PC, LVL_ALO.17, U$3.PA3
- new net H_A5: CARTRIDGE.PD, LVL_ALO.16, U$3.PB3
- new net H_A6: CARTRIDGE.PE, LVL_ALO.15, U$3.PA4
- new net H_A7: CARTRIDGE.PF, LVL_ALO.14, U$3.PB4
- new net H_A8: CARTRIDGE.PH, LVL_AHI.21, U$3.PA5
- new net H_A9: CARTRIDGE.PJ, LVL_AHI.20, U$3.PB5
- new net H_CLK: CARTRIDGE.PS, U$3.PA9
- new net H_D0: CARTRIDGE.P10, LVL_D.21, U$3.PB9
- new net H_D1: CARTRIDGE.P9, LVL_D.20, U$3.PA10
- new net H_D2: CARTRIDGE.P8, LVL_D.19, U$3.PB10
- new net H_D3: CARTRIDGE.PL, LVL_D.18, U$3.PA11
- new net H_D4: CARTRIDGE.P6, LVL_D.17, U$3.PB11
- new net H_D5: CARTRIDGE.P7, LVL_D.16, U$3.PA12
- new net H_D6: CARTRIDGE.P11, LVL_D.15, U$3.PB12
- new net H_D7: CARTRIDGE.PM, LVL_D.14, U$3.PA13
- new net H_R/!W!: CARTRIDGE.PR, U$3.PB17
- new net H_RD4: CARTRIDGE.PA, U$3.PB15
- new net H_RD5: CARTRIDGE.P14, U$3.PA16
- new net H_REF: U$3.PB16
- net +3V3: now also U$4.1, U$4.5, U$6.1, U$6.5, U$7.1, U$7.5, U$8.1, U$8.5, U$9.1, U$9.5
- net +5V: now also U$4.6, U$6.6, U$7.6, U$8.6, U$9.6
- net GND: now also U$3.SHIELD1, U$3.SHIELD2, U$3.SHIELD3, U$3.SHIELD4, U$3.SHIELD5, U$3.SHIELD6, U$4.2, U$6.2, U$7.2, U$8.2, U$9.2
